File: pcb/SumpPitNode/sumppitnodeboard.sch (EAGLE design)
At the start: 28 parts, among them IC1 7805T

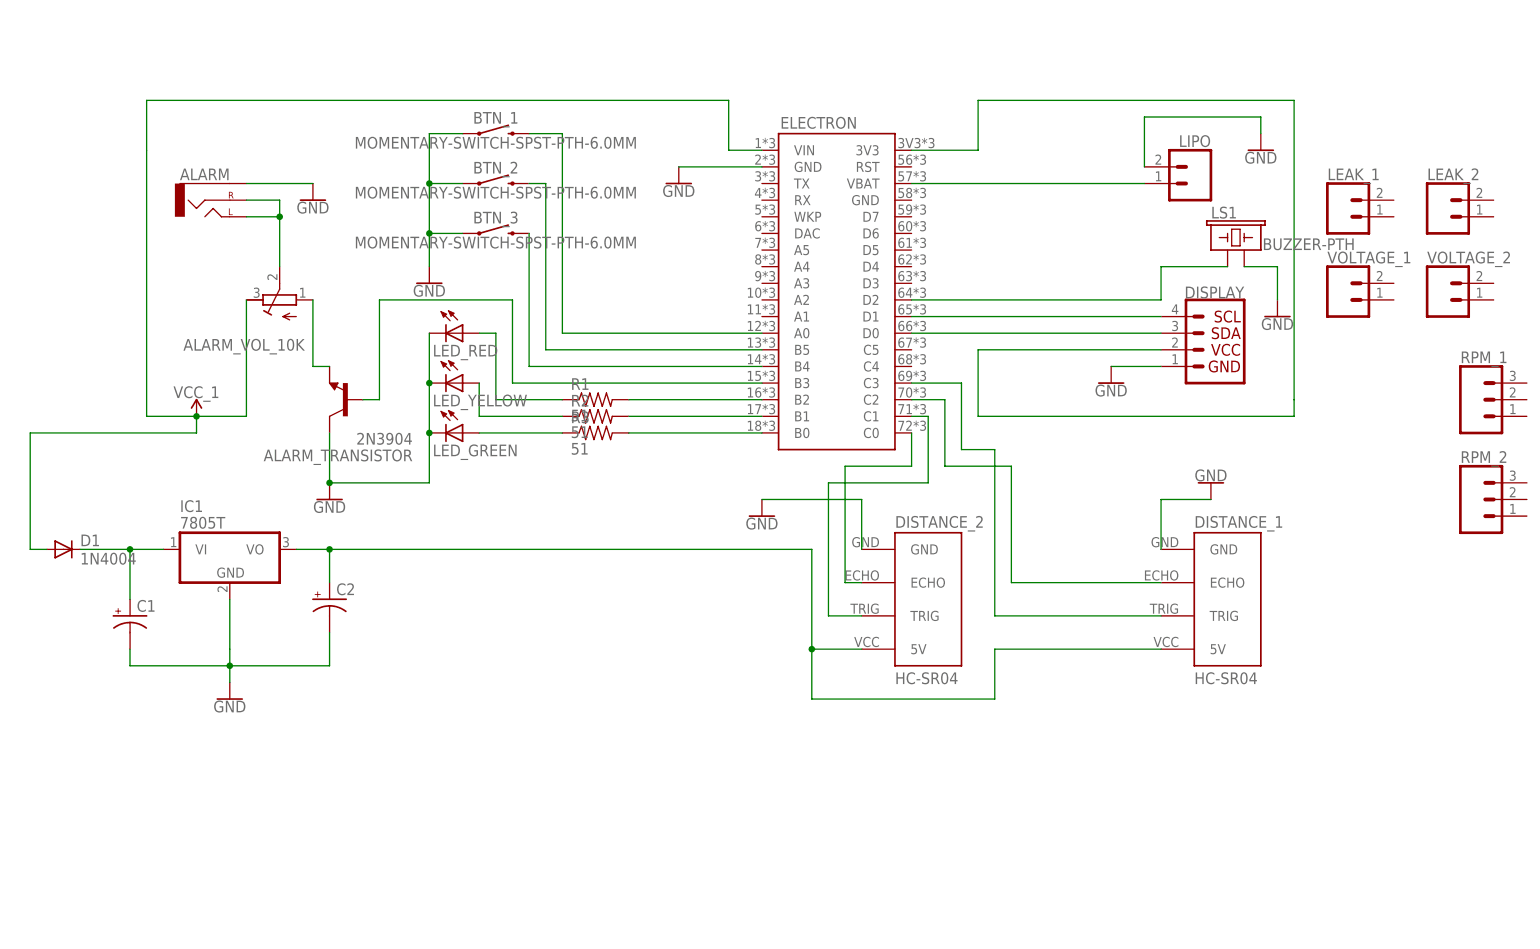
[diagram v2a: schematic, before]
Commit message: connect rpm, voltage with voltage dividers (12v->2.8v)
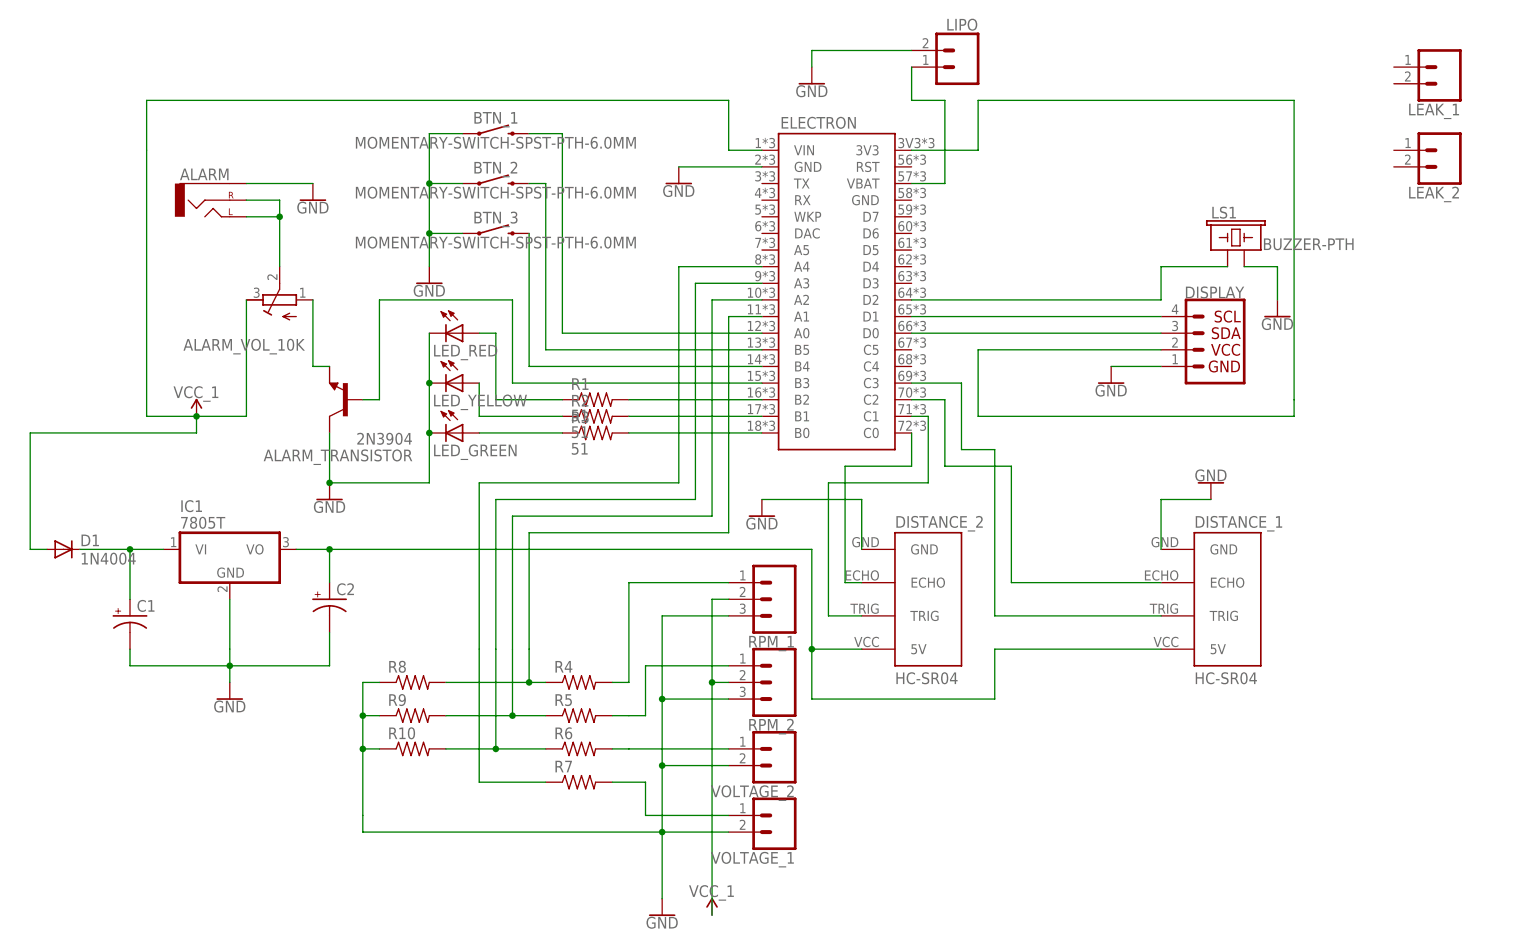
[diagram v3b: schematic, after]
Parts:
- added R10, R4, R5, R6, R7, R8, R9: (no value), resistor:R-US_0204/5
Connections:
- new net N$24: R6.2, VOLTAGE_2.1
- new net N$25: R5.2, RPM_2.1
- new net N$26: R4.2, RPM_1.1
- new net N$27: R7.2, VOLTAGE_1.1
- new net N$28: ELECTRON.A1, R4.1, R8.2
- new net N$29: ELECTRON.A2, R5.1, R9.2
- new net N$30: ELECTRON.A3, R10.2, R6.1
- new net N$31: ELECTRON.A4, R7.1
- new net VCC_1: RPM_1.2, RPM_2.2
- net GND: now also R10.1, R8.1, R9.1, RPM_1.3, RPM_2.3, VOLTAGE_1.2, VOLTAGE_2.2
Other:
- moved on the sheet: LEAK_1, LEAK_2, LIPO, RPM_1, RPM_2, VOLTAGE_1, VOLTAGE_2

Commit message: Move 5v to a better place.
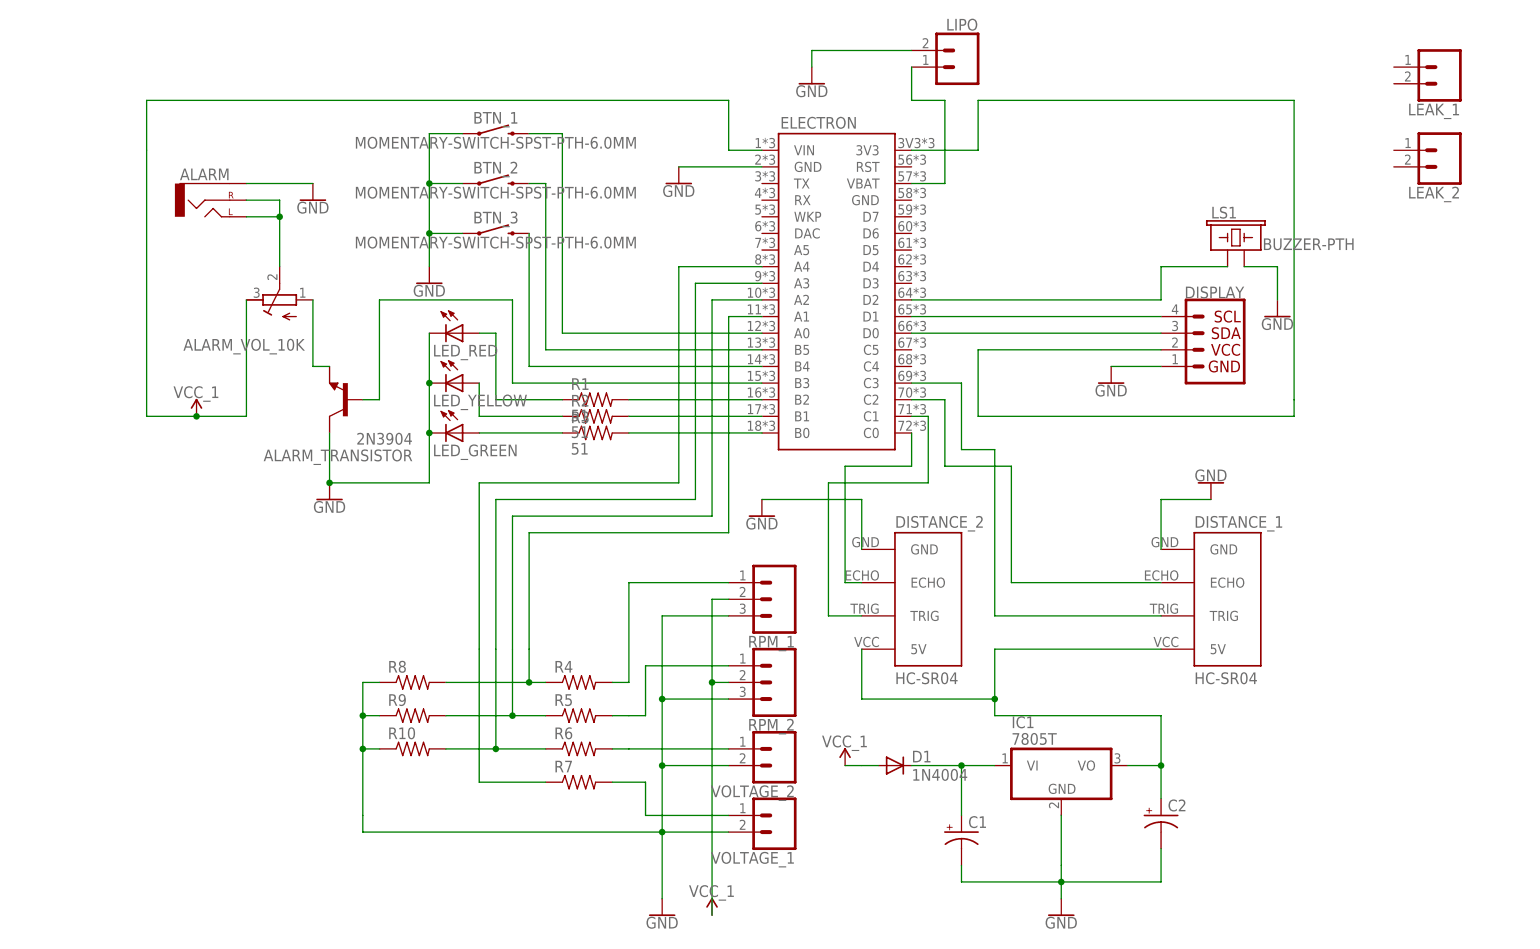
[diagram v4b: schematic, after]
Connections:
- net B$11: no longer D1.A
- net VCC_1: now also D1.A
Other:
- moved on the sheet: C1, C2, D1, IC1
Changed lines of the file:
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@@
 <part name="R9" library="resistor" library_urn="urn:adsk.eagle:library:348" deviceset="R-US_" device="0204/5" package3d_urn="urn:adsk.eagle:package:25955/1"/>
 <part name="R10" library="resistor" library_urn="urn:adsk.eagle:library:348" deviceset="R-US_" device="0204/5" package3d_urn="urn:adsk.eagle:package:25955/1"/>
+<part name="VCC_12V2" library="SparkFun-PowerSymbols" library_urn="urn:adsk.eagle:library:530" deviceset="VCC_1" device=""/>
 </parts>
 <sheets>
@@
 <instance part="GND5" gate="1" x="-96.52" y="60.96"/>
 <instance part="GND6" gate="1" x="7.62" y="45.72"/>
-<instance part="IC1" gate="A1" x="-127" y="20.32"/>
-<instance part="D1" gate="1" x="-152.4" y="20.32"/>
-<instance part="C1" gate="G$1" x="-142.24" y="10.16"/>
-<instance part="C2" gate="G$1" x="-111.76" y="12.7"/>
-<instance part="GND7" gate="1" x="-127" y="-2.54"/>
+<instance part="IC1" gate="A1" x="0" y="-12.7"/>
+<instance part="D1" gate="1" x="-25.4" y="-12.7"/>
+<instance part="C1" gate="G$1" x="-15.24" y="-22.86"/>
+<instance part="C2" gate="G$1" x="15.24" y="-20.32"/>
+<instance part="GND7" gate="1" x="0" y="-35.56"/>
 <instance part="GND8" gate="1" x="22.86" y="30.48" rot="R180"/>
 <instance part="GND9" gate="1" x="-45.72" y="25.4"/>
@@
 <instance part="R9" gate="G$1" x="-99.06" y="-5.08"/>
 <instance part="R10" gate="G$1" x="-99.06" y="-10.16"/>
+<instance part="VCC_12V2" gate="G$2" x="-33.02" y="-12.7"/>
 </instances>
 <busses>
@@
 <pinref part="ELECTRON" gate="G$1" pin="VIN"/>
 <wire x1="-50.8" y1="81.28" x2="-45.72" y2="81.28" width="0.1524" layer="91"/>
-<pinref part="D1" gate="1" pin="A"/>
-<wire x1="-154.94" y1="20.32" x2="-157.48" y2="20.32" width="0.1524" layer="91"/>
-<wire x1="-157.48" y1="20.32" x2="-157.48" y2="38.1" width="0.1524" layer="91"/>
-<wire x1="-157.48" y1="38.1" x2="-132.08" y2="38.1" width="0.1524" layer="91"/>
-<wire x1="-132.08" y1="38.1" x2="-132.08" y2="40.64" width="0.1524" layer="91"/>
 </segment>
 </net>
@@
 <segment>
 <pinref part="IC1" gate="A1" pin="GND"/>
-<wire x1="-127" y1="12.7" x2="-127" y2="5.08" width="0.1524" layer="91"/>
+<wire x1="0" y1="-20.32" x2="0" y2="-27.94" width="0.1524" layer="91"/>
 <pinref part="C2" gate="G$1" pin="-"/>
-<wire x1="-111.76" y1="7.62" x2="-111.76" y2="2.54" width="0.1524" layer="91"/>
-<wire x1="-111.76" y1="2.54" x2="-127" y2="2.54" width="0.1524" layer="91"/>
-<wire x1="-127" y1="2.54" x2="-127" y2="5.08" width="0.1524" layer="91"/>
-<wire x1="-127" y1="2.54" x2="-142.24" y2="2.54" width="0.1524" layer="91"/>
-<junction x="-127" y="2.54"/>
+<wire x1="15.24" y1="-25.4" x2="15.24" y2="-30.48" width="0.1524" layer="91"/>
+<wire x1="15.24" y1="-30.48" x2="0" y2="-30.48" width="0.1524" layer="91"/>
+<wire x1="0" y1="-30.48" x2="0" y2="-27.94" width="0.1524" layer="91"/>
+<wire x1="0" y1="-30.48" x2="-15.24" y2="-30.48" width="0.1524" layer="91"/>
+<junction x="0" y="-30.48"/>
 <pinref part="C1" gate="G$1" pin="-"/>
-<wire x1="-142.24" y1="2.54" x2="-142.24" y2="5.08" width="0.1524" layer="91"/>
+<wire x1="-15.24" y1="-30.48" x2="-15.24" y2="-27.94" width="0.1524" layer="91"/>
 <pinref part="GND7" gate="1" pin="GND"/>
-<wire x1="-127" y1="0" x2="-127" y2="2.54" width="0.1524" layer="91"/>
+<wire x1="0" y1="-33.02" x2="0" y2="-30.48" width="0.1524" layer="91"/>
 </segment>
 <segment>
@@
 <pinref part="D1" gate="1" pin="C"/>
 <pinref part="IC1" gate="A1" pin="VI"/>
-<wire x1="-149.86" y1="20.32" x2="-142.24" y2="20.32" width="0.1524" layer="91"/>
+<wire x1="-22.86" y1="-12.7" x2="-15.24" y2="-12.7" width="0.1524" layer="91"/>
 <pinref part="C1" gate="G$1" pin="+"/>
-<wire x1="-142.24" y1="20.32" x2="-137.16" y2="20.32" width="0.1524" layer="91"/>
-<wire x1="-142.24" y1="20.32" x2="-142.24" y2="12.7" width="0.1524" layer="91"/>
-<junction x="-142.24" y="20.32"/>
-</segment>
-</net>
-<net name="N$23" class="0">
-<segment>
-<pinref part="DISTANCE_2" gate="J_ULTRASONIC" pin="5V"/>
-<wire x1="-30.48" y1="5.08" x2="-38.1" y2="5.08" width="0.1524" layer="91"/>
-<wire x1="-38.1" y1="5.08" x2="-38.1" y2="20.32" width="0.1524" layer="91"/>
-<pinref part="DISTANCE_1" gate="J_ULTRASONIC" pin="5V"/>
-<wire x1="15.24" y1="5.08" x2="-10.16" y2="5.08" width="0.1524" layer="91"/>
-<wire x1="-10.16" y1="5.08" x2="-10.16" y2="-2.54" width="0.1524" layer="91"/>
-<wire x1="-10.16" y1="-2.54" x2="-38.1" y2="-2.54" width="0.1524" layer="91"/>
-<wire x1="-38.1" y1="-2.54" x2="-38.1" y2="5.08" width="0.1524" layer="91"/>
-<junction x="-38.1" y="5.08"/>
-<pinref part="IC1" gate="A1" pin="VO"/>
-<wire x1="-116.84" y1="20.32" x2="-111.76" y2="20.32" width="0.1524" layer="91"/>
-<pinref part="C2" gate="G$1" pin="+"/>
-<wire x1="-111.76" y1="15.24" x2="-111.76" y2="20.32" width="0.1524" layer="91"/>
-<wire x1="-38.1" y1="20.32" x2="-111.76" y2="20.32" width="0.1524" layer="91"/>
-<junction x="-111.76" y="20.32"/>
+<wire x1="-15.24" y1="-12.7" x2="-10.16" y2="-12.7" width="0.1524" layer="91"/>
+<wire x1="-15.24" y1="-12.7" x2="-15.24" y2="-20.32" width="0.1524" layer="91"/>
+<junction x="-15.24" y="-12.7"/>
 </segment>
 </net>
@@
 <pinref part="RPM_1" gate="J$1" pin="2"/>
 <wire x1="-53.34" y1="12.7" x2="-50.8" y2="12.7" width="0.1524" layer="91"/>
+</segment>
+<segment>
+<pinref part="D1" gate="1" pin="A"/>
+<wire x1="-27.94" y1="-12.7" x2="-30.48" y2="-12.7" width="0.1524" layer="91"/>
+<pinref part="VCC_12V2" gate="G$2" pin="VCC_1"/>
+<wire x1="-30.48" y1="-12.7" x2="-33.02" y2="-12.7" width="0.1524" layer="91"/>
 </segment>
 </net>
@@
 </segment>
 </net>
+<net name="N$33" class="0">
+<segment>
+<pinref part="IC1" gate="A1" pin="VO"/>
+<wire x1="10.16" y1="-12.7" x2="15.24" y2="-12.7" width="0.1524" layer="91"/>
+<pinref part="C2" gate="G$1" pin="+"/>
+<wire x1="15.24" y1="-17.78" x2="15.24" y2="-12.7" width="0.1524" layer="91"/>
+<wire x1="15.24" y1="-12.7" x2="15.24" y2="-5.08" width="0.1524" layer="91"/>
+<junction x="15.24" y="-12.7"/>
+<wire x1="15.24" y1="-5.08" x2="-10.16" y2="-5.08" width="0.1524" layer="91"/>
+<pinref part="DISTANCE_2" gate="J_ULTRASONIC" pin="5V"/>
+<pinref part="DISTANCE_1" gate="J_ULTRASONIC" pin="5V"/>
+<wire x1="15.24" y1="5.08" x2="-10.16" y2="5.08" width="0.1524" layer="91"/>
+<wire x1="-10.16" y1="5.08" x2="-10.16" y2="-2.54" width="0.1524" layer="91"/>
+<wire x1="-10.16" y1="-2.54" x2="-30.48" y2="-2.54" width="0.1524" layer="91"/>
+<wire x1="-10.16" y1="-5.08" x2="-10.16" y2="-2.54" width="0.1524" layer="91"/>
+<junction x="-10.16" y="-2.54"/>
+<wire x1="-30.48" y1="5.08" x2="-30.48" y2="-2.54" width="0.1524" layer="91"/>
+</segment>
+</net>
